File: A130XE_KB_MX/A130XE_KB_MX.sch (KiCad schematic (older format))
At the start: 78 parts, among them J1 Conn_01x32, J2 Conn_01x02_Male, J3 Conn_01x03_Male, J4 Conn_01x03_Male, J5 34 pin ribbon keyboard cable, SW1 KS_RESET, SW10 K_5, SW11 K_I, SW12 K_T, SW13 K_G, SW14 K_SPACE, SW15 K_B, SW16 K_K, SW17 KS_SELECT, SW18 K_4, SW19 K_O, SW2 K_6, SW20 K_R, SW21 K_F, SW22 K_M, SW23 K_V, SW24 K_L, SW25 K_3, SW26 K_P, SW27 K_E, SW28 K_D, SW29 KS_START, SW3 K_U, SW30 K_comma, SW31 K_comdot, SW32 K_C, SW33 K_dot, SW34 K_2, SW35 K_minus, SW36 K_W, SW37 K_S, SW38 K_X, SW39 K_plus, SW4 K_Y, SW40 K_1, SW41 K_equal, SW42 K_Q, SW43 K_A, SW44 K_slash, SW45 K_asterisk, SW46 K_Z, SW47 K_ATARI, SW48 K_ESC, SW49 K_RETURN, SW5 K_H, SW50 K_TAB, SW51 K_CAPS, SW52 K_CTRL, SW53 K_LSHIFT, SW54 K_RSHIFT, SW55 K_BRK, SW56 K_DEL, SW57 K_GT, SW58 K_LT, SW59 K_0, SW6 K_N, SW60 K_9, SW61 K_8, SW62 K_7, SW63 K_SPACE_1, SW64 K_SPACE_2, SW65 K_F1, SW66 K_F2, SW67 K_F3, SW68 K_F4, SW7 KS_HELP, SW8 K_J, SW9 KS_OPTION

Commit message: Updated connector name
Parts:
- J1: footprint RetroBitLab:FFC-1.25mm-RA-5204403245 -> RetroBitLab:MOLEX-FFC-1.25mm-RA-52044-3245
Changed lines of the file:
@@
 F 0 "J1" H 10700 6750 50  0000 L CNN
 F 1 "Conn_01x32" H 9600 6850 50  0000 L CNN
-F 2 "RetroBitLab:FFC-1.25mm-RA-5204403245" H 10600 6750 50  0001 C CNN
+F 2 "RetroBitLab:MOLEX-FFC-1.25mm-RA-52044-3245" H 10600 6750 50  0001 C CNN
 F 3 "~" H 10600 6750 50  0001 C CNN
 	1    10600 6750

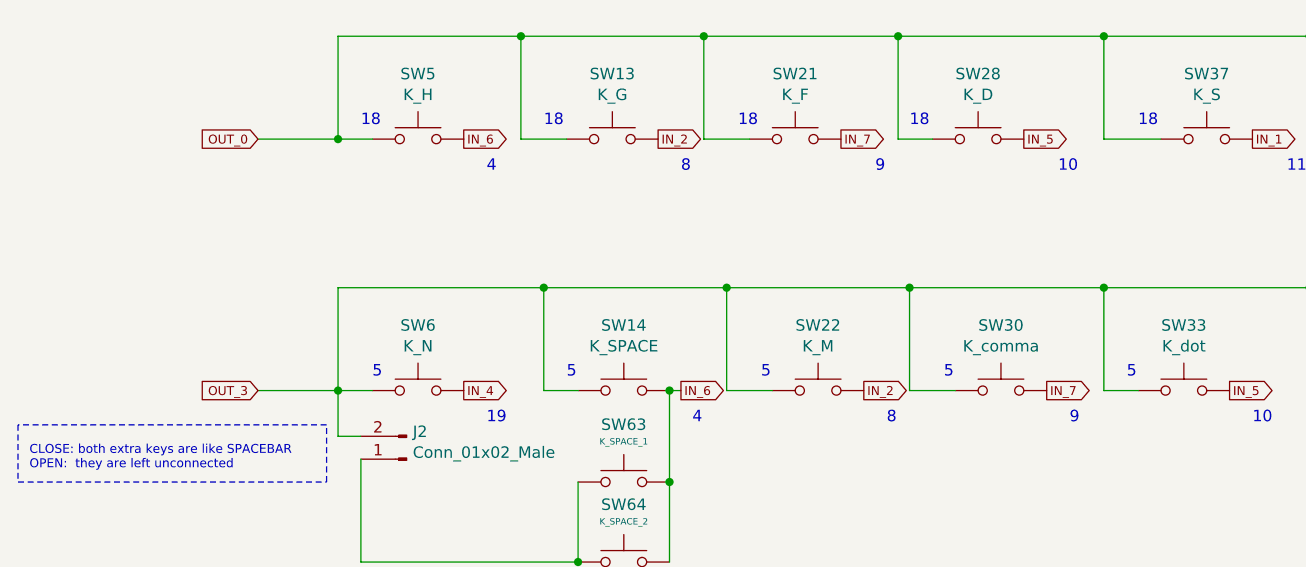
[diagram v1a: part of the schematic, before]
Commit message: New render for extra hole in the function keys (even if not needed really) and the spacebar 9U as alternative for modern spacebar 6.25U plus the other two keys
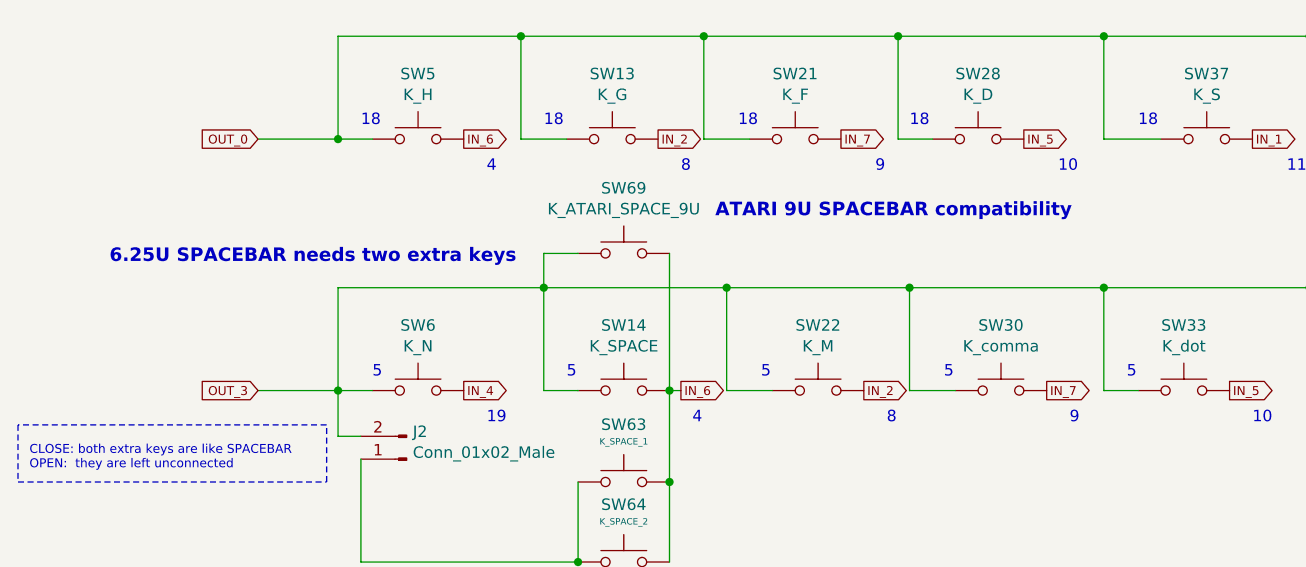
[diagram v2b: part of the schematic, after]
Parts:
- added SW69: K_ATARI_SPACE_9U, RetroBitLab:SW_Cherry_MX1A_9u_PCB_3d, symbol Switch:SW_Push
- SW1, SW17, SW29, SW7, SW9: footprint RetroBitLab:SW_Cherry_MX1A_1.50u_PCB_3d -> RetroBitLab:SW_Cherry_MX1A_1.50u_ATARI_XE_PCB_3d
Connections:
- net IN_6: now also SW69.2
- net OUT_3: now also SW69.1
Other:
- note added: "6.25U SPACEBAR needs two extra keys"
- note added: "ATARI 9U SPACEBAR compatibility"
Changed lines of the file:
@@
 Sheet 1 1
 Title "ATARI XE KEYBOARD PCB "
-Date "2021-01-30"
+Date "2021-04-03"
 Rev "2.0"
 Comp "RetroBitLab Tech Guy"
@@
 F 0 "SW1" H 10700 3435 50  0000 C CNN
 F 1 "KS_RESET" H 10700 3344 50  0000 C CNN
-F 2 "RetroBitLab:SW_Cherry_MX1A_1.50u_PCB_3d" H 10700 3350 50  0001 C CNN
+F 2 "RetroBitLab:SW_Cherry_MX1A_1.50u_ATARI_XE_PCB_3d" H 10700 3350 50  0001 C CNN
 F 3 "" H 10700 3350 50  0001 C CNN
 	1    10700 3150
@@
 F 0 "SW9" H 11600 3435 50  0000 C CNN
 F 1 "KS_OPTION" H 11600 3344 50  0000 C CNN
-F 2 "RetroBitLab:SW_Cherry_MX1A_1.50u_PCB_3d" H 11600 3350 50  0001 C CNN
+F 2 "RetroBitLab:SW_Cherry_MX1A_1.50u_ATARI_XE_PCB_3d" H 11600 3350 50  0001 C CNN
 F 3 "" H 11600 3350 50  0001 C CNN
 	1    11600 3150
@@
 F 0 "SW17" H 12500 3435 50  0000 C CNN
 F 1 "KS_SELECT" H 12500 3344 50  0000 C CNN
-F 2 "RetroBitLab:SW_Cherry_MX1A_1.50u_PCB_3d" H 12500 3350 50  0001 C CNN
+F 2 "RetroBitLab:SW_Cherry_MX1A_1.50u_ATARI_XE_PCB_3d" H 12500 3350 50  0001 C CNN
 F 3 "" H 12500 3350 50  0001 C CNN
 	1    12500 3150
@@
 F 0 "SW29" H 13350 3435 50  0000 C CNN
 F 1 "KS_START" H 13350 3344 50  0000 C CNN
-F 2 "RetroBitLab:SW_Cherry_MX1A_1.50u_PCB_3d" H 13350 3350 50  0001 C CNN
+F 2 "RetroBitLab:SW_Cherry_MX1A_1.50u_ATARI_XE_PCB_3d" H 13350 3350 50  0001 C CNN
 F 3 "" H 13350 3350 50  0001 C CNN
 	1    13350 3150
@@
 F 0 "SW7" H 2450 10335 50  0000 C CNN
 F 1 "KS_HELP" H 2450 10244 50  0000 C CNN
-F 2 "RetroBitLab:SW_Cherry_MX1A_1.50u_PCB_3d" H 2450 10250 50  0001 C CNN
+F 2 "RetroBitLab:SW_Cherry_MX1A_1.50u_ATARI_XE_PCB_3d" H 2450 10250 50  0001 C CNN
 F 3 "" H 2450 10250 50  0001 C CNN
 	1    2450 10050
@@
 Wire Notes Line
 	12250 4600 8900 4600
+$Comp
+L Switch:SW_Push SW69
+U 1 1 6069B9A5
+P 3350 7950
+F 0 "SW69" H 3350 8235 50  0000 C CNN
+F 1 "K_ATARI_SPACE_9U" H 3350 8144 50  0000 C CNN
+F 2 "RetroBitLab:SW_Cherry_MX1A_9u_PCB_3d" H 3350 8150 50  0001 C CNN
+F 3 "" H 3350 8150 50  0001 C CNN
+	1    3350 7950
+	1    0    0    -1
+$EndComp
+Wire Wire Line
+	3150 7950 3000 7950
+Wire Wire Line
+	3000 7950 3000 8100
+Wire Wire Line
+	3550 7950 3550 8550
+Text Notes 3750 7800 0    59   ~ 12
+ATARI 9U SPACEBAR compatibility
+Text Notes 1100 8000 0    59   ~ 12
+6.25U SPACEBAR needs two extra keys
 $EndSCHEMATC
